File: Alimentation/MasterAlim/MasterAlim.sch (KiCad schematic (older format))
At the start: 15 parts, among them J1 Ext-Con, J11 AU Logic, J2 Alim logique

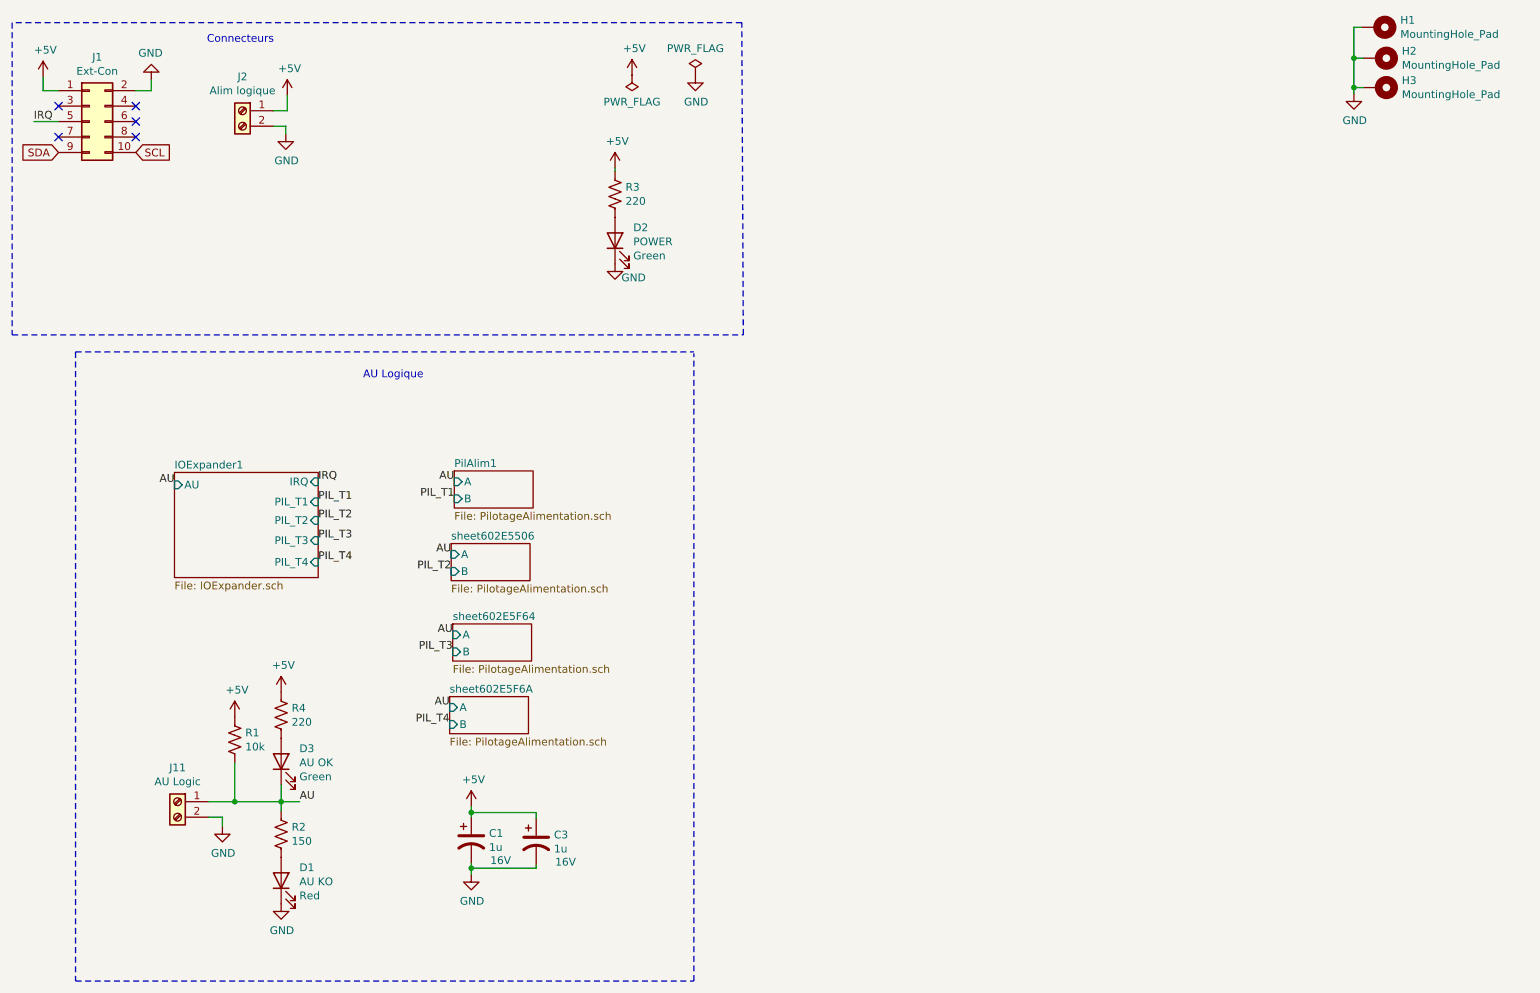
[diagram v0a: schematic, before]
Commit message: Fix Master Alim : affichage statut AU
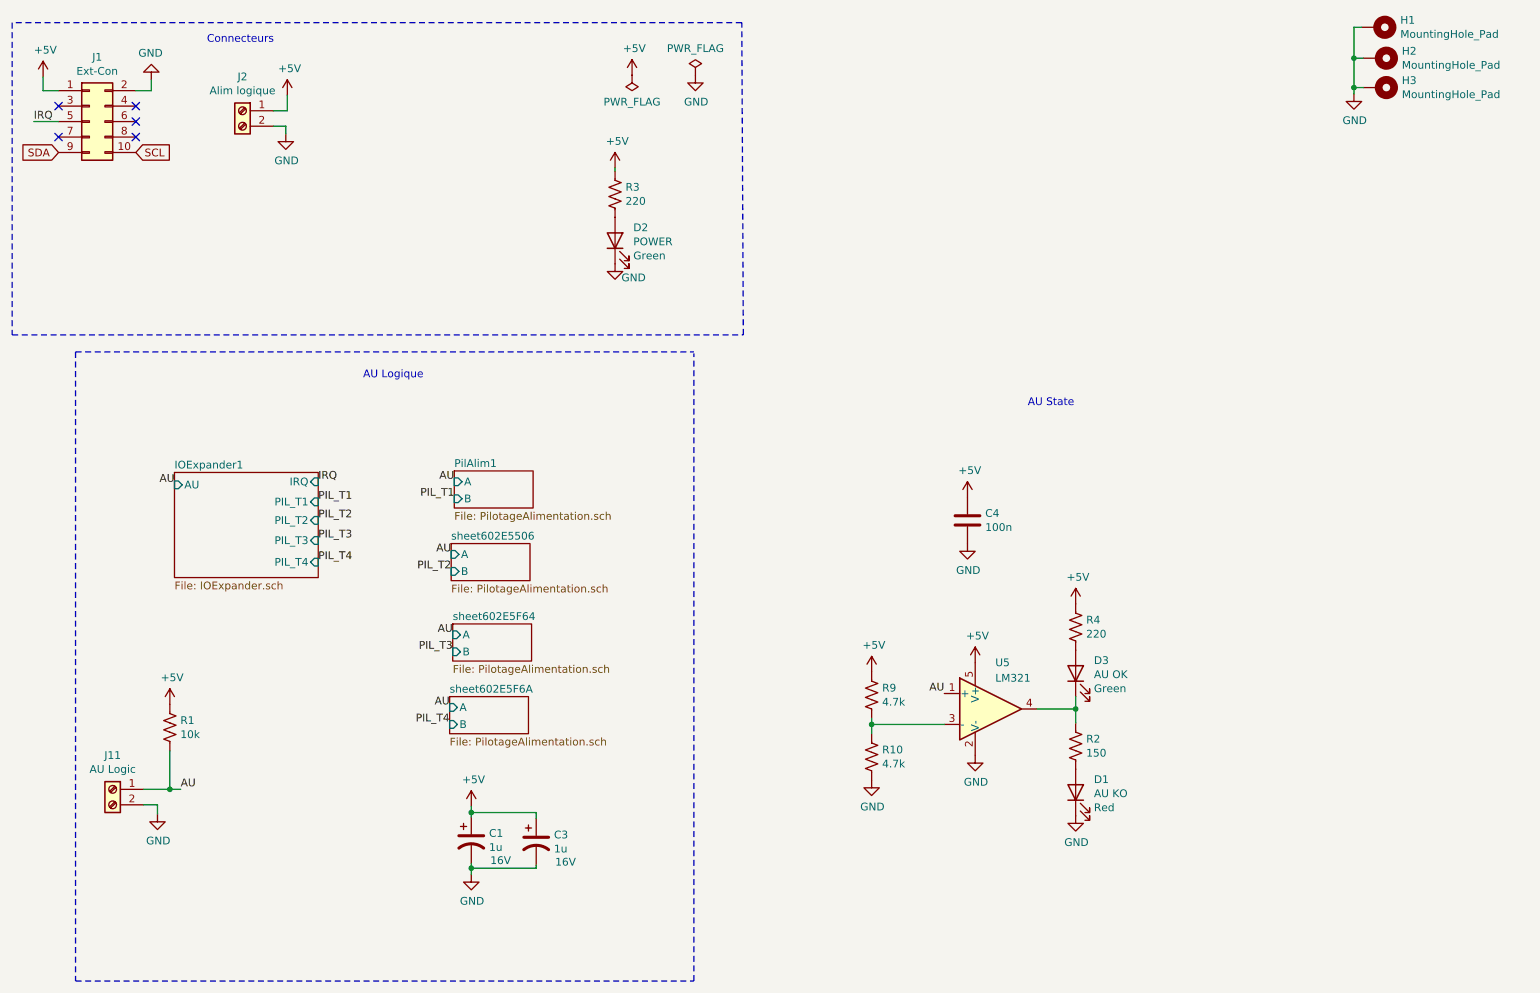
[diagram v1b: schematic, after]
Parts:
- added C4: 100n, Capacitor_SMD:C_0603_1608Metric_Pad1.08x0.95mm_HandSolder, symbol Device:C
- added R10, R9: 4.7k, Resistor_SMD:R_0805_2012Metric_Pad1.20x1.40mm_HandSolder, symbol Device:R_US
- added U5: LM321, Package_TO_SOT_SMD:SOT-23-5, symbol Amplifier_Operational:LM321
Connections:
- net +5V: now also C4.1, R9.1, U5.5 (V+)
- net AU: now also U5.1 (+); no longer D3.1 (K), R2.1
- net GND: now also C4.2, R10.2, U5.2 (V-)
- new net: D3.1 (K), R2.1, U5.4
- new net: R10.1, R9.2, U5.3 (-)
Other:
- note added: "AU State"
- moved on the sheet: D1, D3, J11, R1, R2, R4
